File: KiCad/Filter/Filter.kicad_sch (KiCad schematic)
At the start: 9 parts, among them U1 LTC1067-50

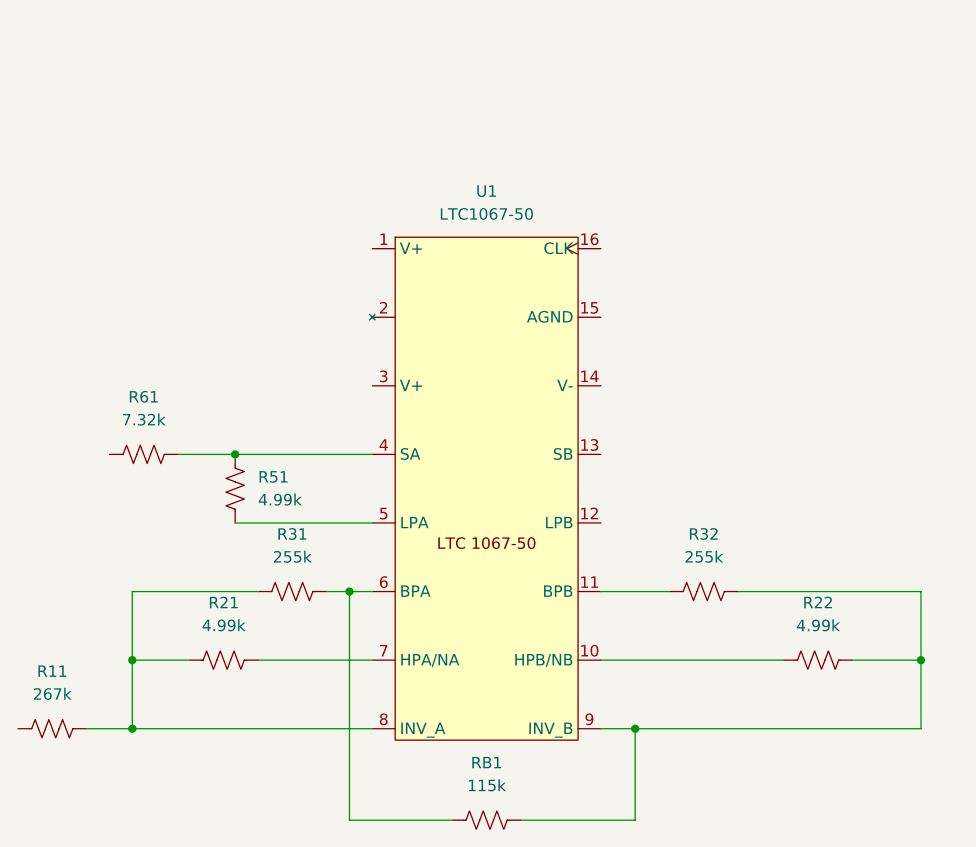
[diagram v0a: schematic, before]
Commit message: Added new sheet to KiCad files. Added MIC5211 folder, a potential LDO for power supply.
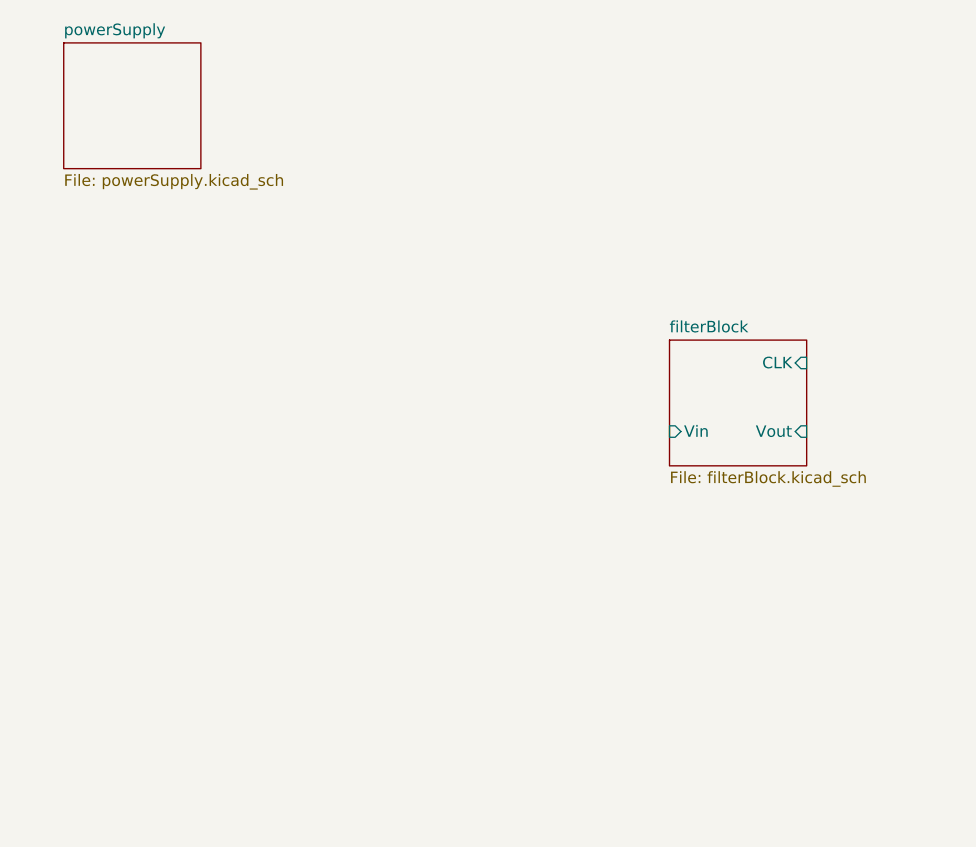
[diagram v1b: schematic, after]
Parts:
- removed R11: 267k, symbol Device:R_US
- removed R21, R22, R51: 4.99k, symbol Device:R_US
- removed R31, R32: 255k, symbol Device:R_US
- removed R61: 7.32k, symbol Device:R_US
- removed RB1: 115k, symbol Device:R_US
- removed U1: LTC1067-50, symbol Misc:LTC1067-50
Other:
- added sheet filterBlock (filterBlock.kicad_sch)
- added sheet powerSupply (powerSupply.kicad_sch)

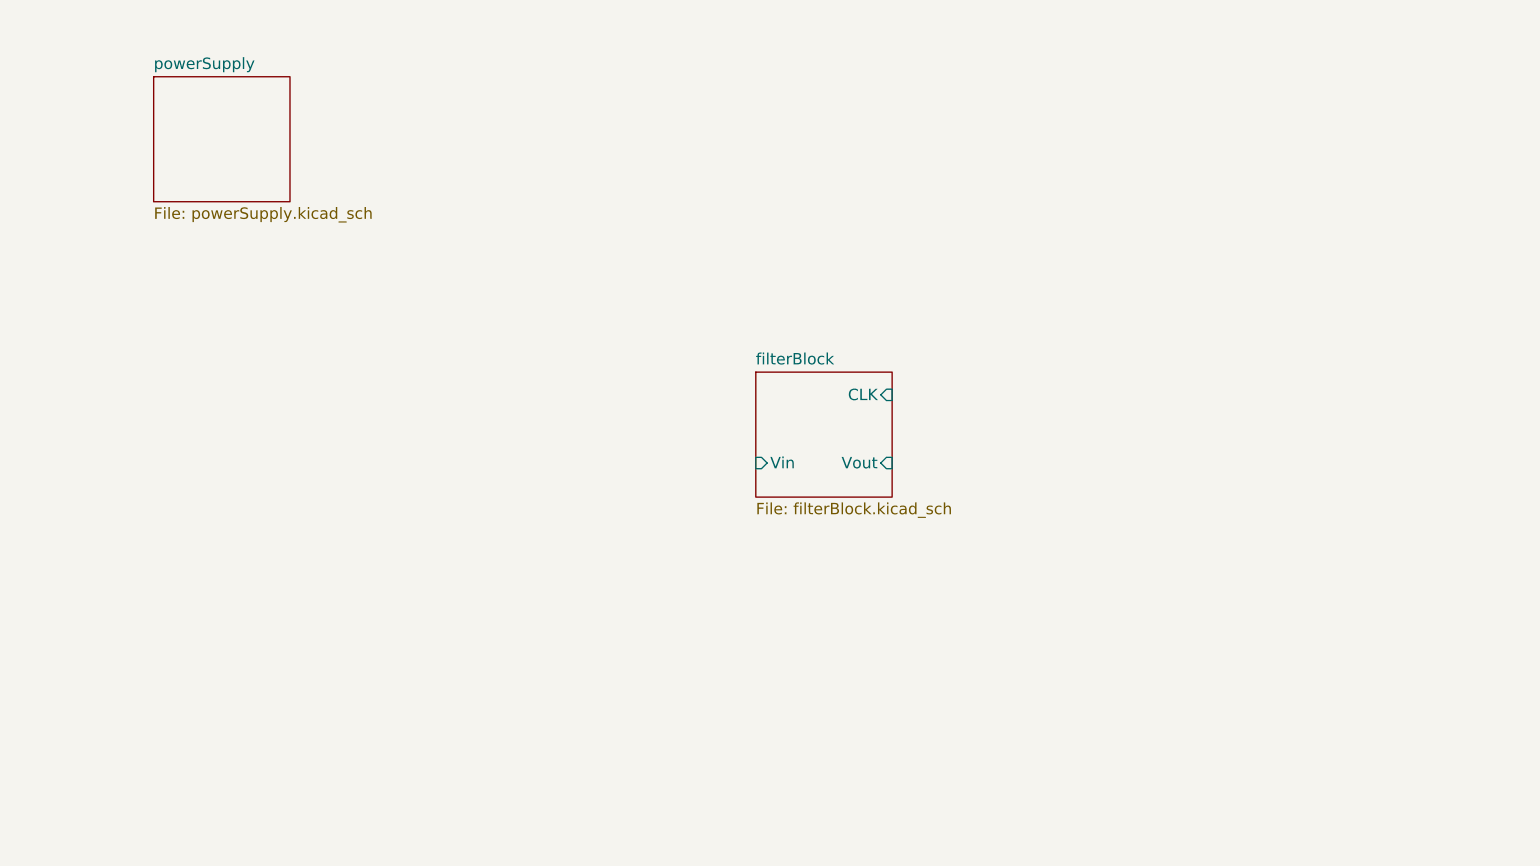
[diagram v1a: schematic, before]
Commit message: VCO circuit added to schematic.
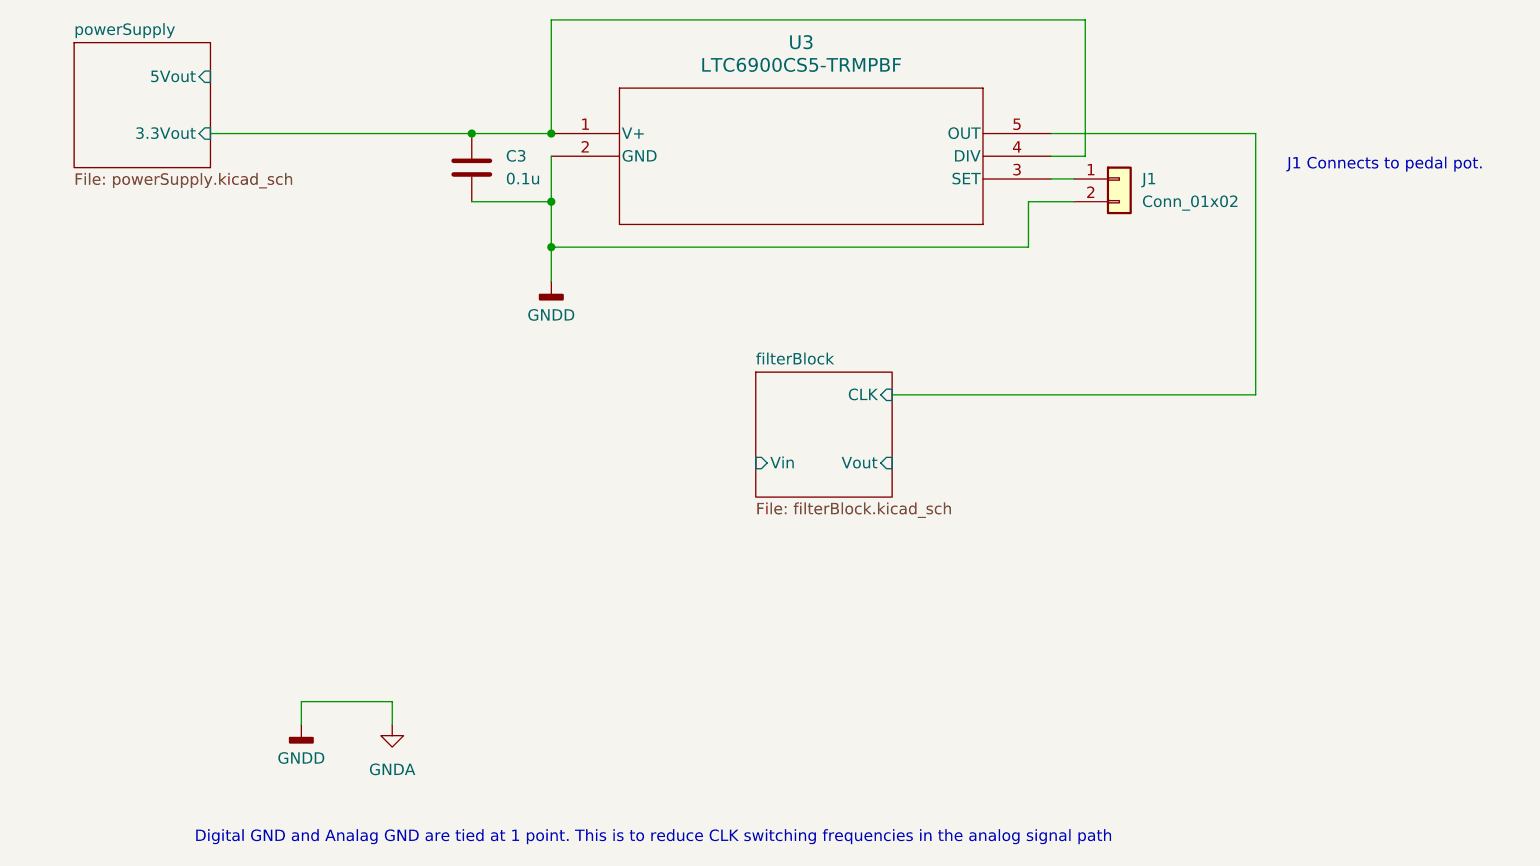
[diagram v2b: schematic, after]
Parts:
- added C3: 0.1u, symbol Device:C
- added J1: Conn_01x02, symbol Connector_Generic:Conn_01x02
- added U3: LTC6900CS5-TRMPBF, SOT-5_S_LIT, symbol Misc:LTC6900CS5-TRMPBF
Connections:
- net filterBlock/CLK: now also U3.5 (OUT)
- new net: J1.1 (Pin_1), U3.3 (SET)
- new net GNDA: C3.2, J1.2 (Pin_2), U3.2 (GND)
- new net powerSupply/3.3Vout: C3.1, U3.1 (V+), U3.4 (DIV)
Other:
- sheet powerSupply ports: added 3.3Vout, 5Vout; removed none
- note added: "Digital GND and Analag GND are tied at 1 point. This is to reduce CLK switching frequencies in the analog signal path"
- note added: "J1 Connects to pedal pot."

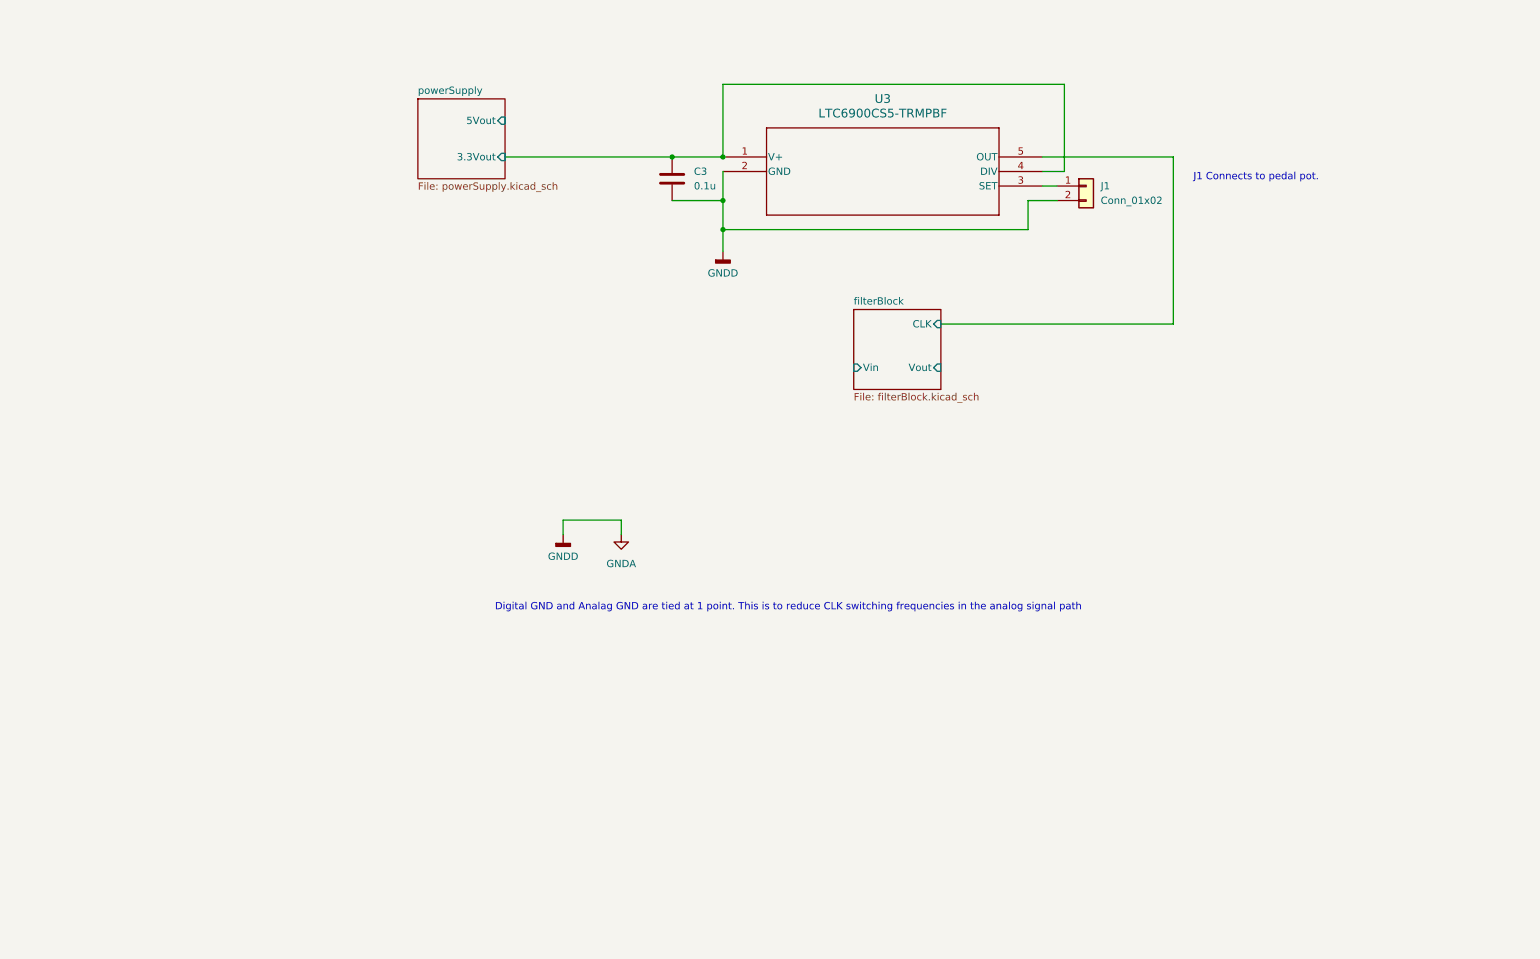
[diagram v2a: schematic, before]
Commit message: Added input jacks and bypass switch. Finished pwr supply except for 9v connection.
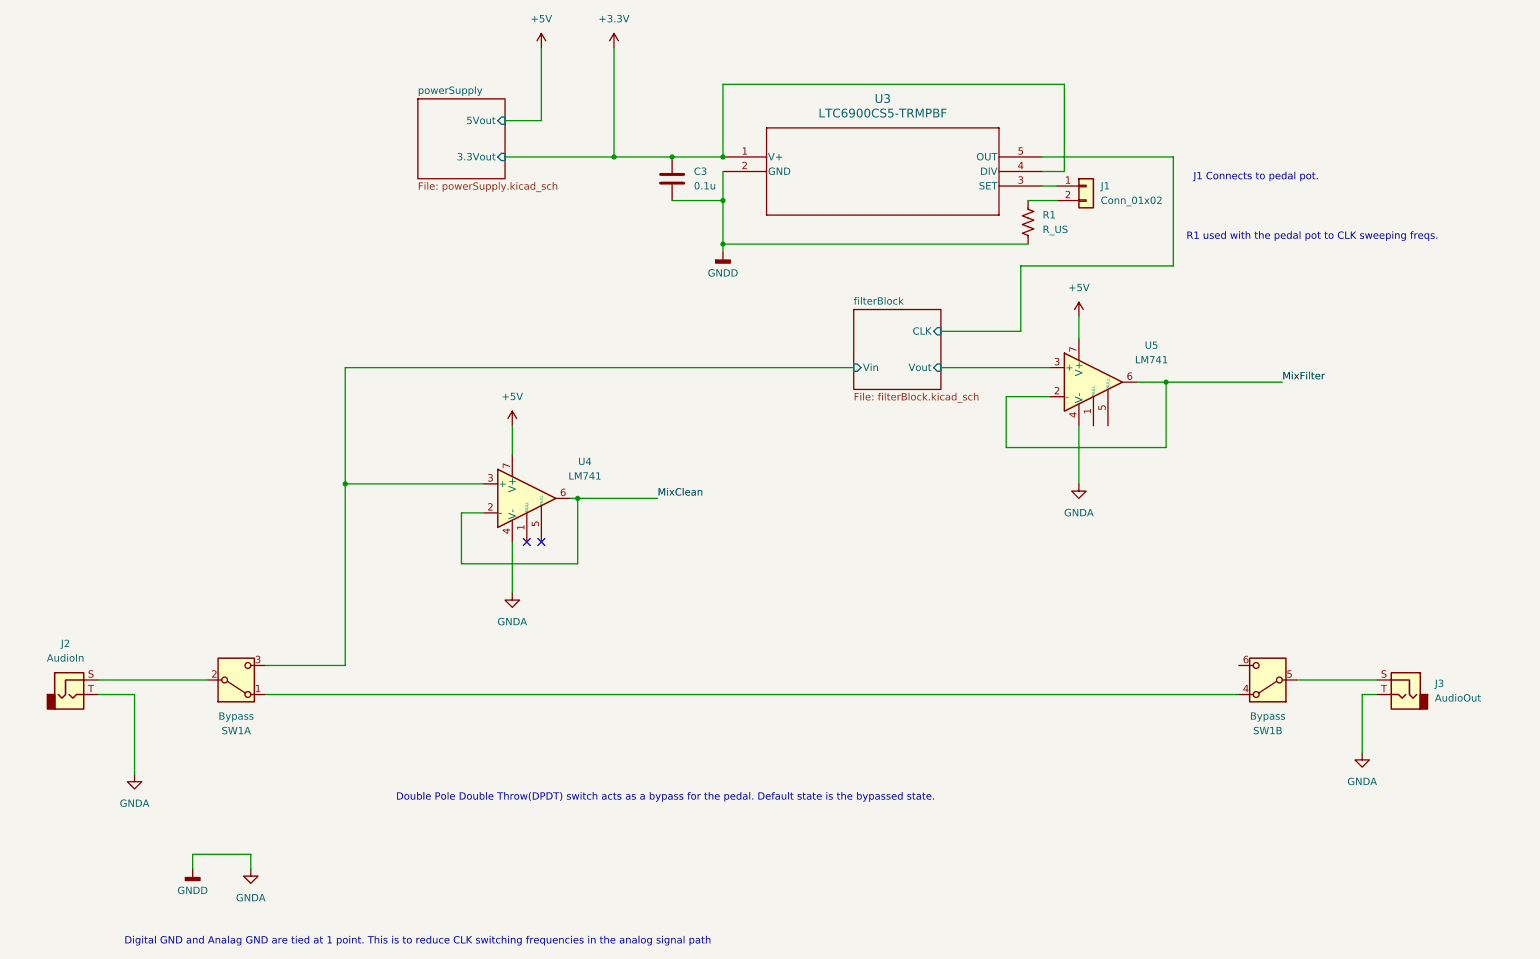
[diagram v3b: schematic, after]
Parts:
- added J2: AudioIn, symbol Connector_Audio:AudioJack2
- added J3: AudioOut, symbol Connector_Audio:AudioJack2
- added R1: R_US, symbol Device:R_US
- added SW1: Bypass, symbol Switch:SW_DPDT_x2
- added U4, U5: LM741, symbol Amplifier_Operational:LM741
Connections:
- net GNDA: now also J2.T, J3.T, R1.1, U4.4 (V-), U5.4 (V-); no longer J1.2 (Pin_2)
- net filterBlock/Vin: now also SW1.3 (C), U4.3 (+)
- net filterBlock/Vout: now also U5.3 (+)
- net powerSupply/3.3Vout renamed +3.3V
- new net: J1.2 (Pin_2), R1.2
- new net: J2.S, SW1.2 (B)
- new net: SW1.1 (A), SW1.4 (A)
- new net: J3.S, SW1.5 (B)
- new net +5V: U4.7 (V+), U5.7 (V+)
- new net MixClean: U4.2 (-), U4.6
- new net MixFilter: U5.2 (-), U5.6
- no-connect marks 0 -> 2
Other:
- note added: "Double Pole Double Throw(DPDT) switch acts as a bypass for the pedal. Default state is the bypassed state."
- note added: "R1 used with the pedal pot to CLK sweeping freqs."

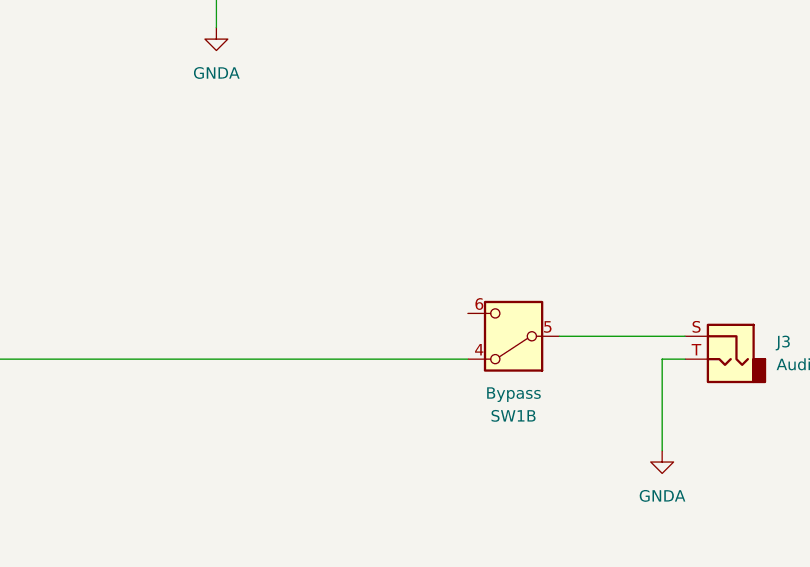
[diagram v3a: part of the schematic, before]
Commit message: Added DC blocking cap
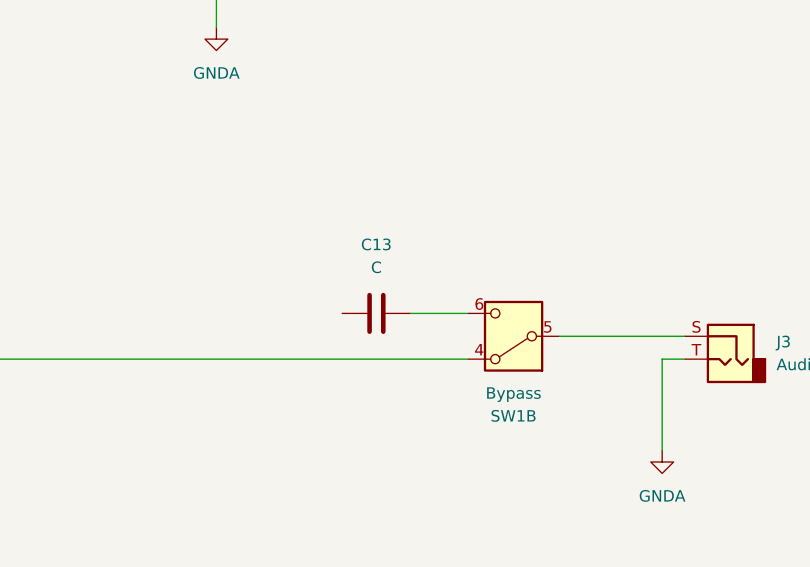
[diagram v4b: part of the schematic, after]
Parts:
- added C13: C, symbol Device:C
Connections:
- net at SW1.6 (C): now also C13.2
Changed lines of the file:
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@@
+	(wire
+		(pts
+			(xy 223.52 133.35) (xy 229.87 133.35)
+		)
+		(stroke
+			(width 0)
+			(type default)
+		)
+	)
 	(wire
 		(pts
@@
 					(unit 1)
 				)
+			)
+		)
+	)
+	(symbol
+		(lib_id "Device:C")
+		(at 219.71 133.35 90)
+		(unit 1)
+		(exclude_from_sim no)
+		(in_bom yes)
+		(on_board yes)
+		(dnp no)
+		(fields_autoplaced yes)
+		(property "Reference" "C13"
+			(at 219.71 125.73 90)
+			(effects
+				(font
+					(size 1.27 1.27)
+				)
+			)
+		)
+		(property "Value" "C"
+			(at 219.71 128.27 90)
+			(effects
+				(font
+					(size 1.27 1.27)
+				)
+			)
+		)
+		(property "Footprint" ""
+			(at 223.52 132.3848 0)
+			(effects
+				(font
+					(size 1.27 1.27)
+				)
+				(hide yes)
+			)
+		)
+		(property "Datasheet" "~"
+			(at 219.71 133.35 0)
+			(effects
+				(font
+					(size 1.27 1.27)
+				)
+				(hide yes)
+			)
+		)
+		(property "Description" "Unpolarized capacitor"
+			(at 219.71 133.35 0)
+			(effects
+				(font
+					(size 1.27 1.27)
+				)
+				(hide yes)
+			)
+		)
+		(pin "1"
+		)
+		(pin "2"
+		)
+		(instances
+			(project ""
+				(path "/8ea2dc21-a8e6-4e4a-8986-17442369c6c0"
+					(reference "C13")
+					(unit 1)
+				)

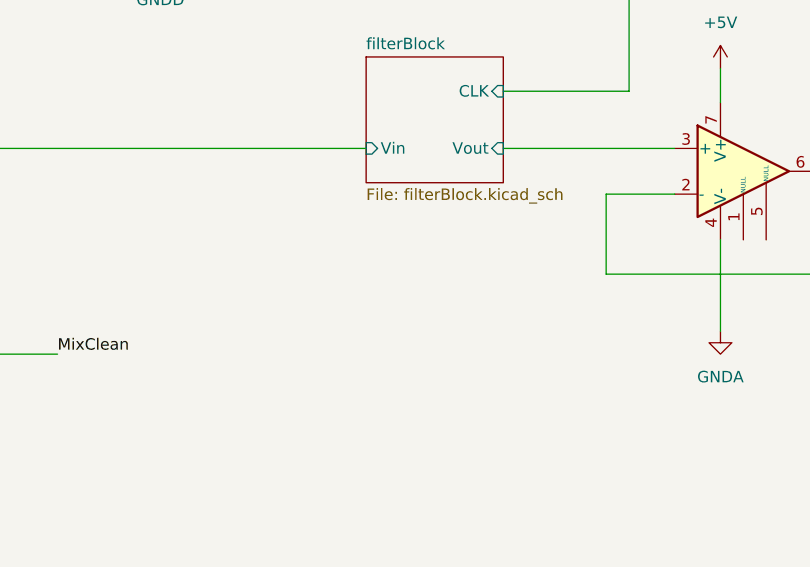
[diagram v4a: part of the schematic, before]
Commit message: Added not in schematic. Need to consider DC Bias points.
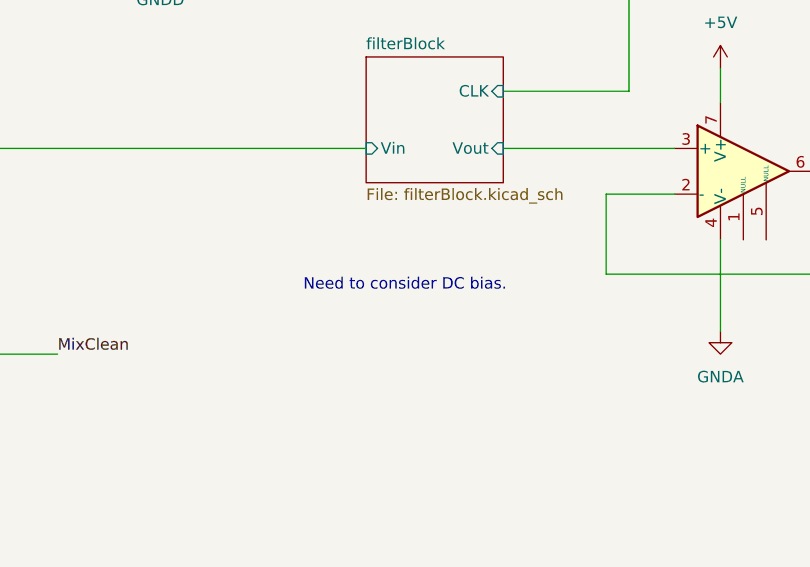
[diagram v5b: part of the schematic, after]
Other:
- note added: "Need to consider DC bias."
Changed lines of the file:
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@@
+		)
+	)
+	(text "Need to consider DC bias."
+		(exclude_from_sim no)
+		(at 166.878 96.52 0)
+		(effects
+			(font
+				(size 1.27 1.27)
+			)
 		)
 	)
